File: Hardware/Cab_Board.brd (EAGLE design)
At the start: 152.9 x 71.1 mm, 158 parts, among them J6 3PCV-03-006, SW1 MF-SW-TACT-4.2MM, SW2 MF-SW-TACT-4.2MM, SW3 MF-SW-TACT-4.2MM, U1 P8X32A-Q44, U10 MAX31855KASA+, U11 MAX31855KASA+, U12 G3VM-61GR2(TR05), U13 G3VM-61GR2(TR05), U14 CD74HC595M96, U15 G3VM-61GR2(TR05), U16 CD74HC165M96, U17 G3VM-61GR2(TR05), U18 G3VM-61GR2(TR05), U19 G3VM-61GR2(TR05), U2 G3VM-61GR2(TR05), U20 G3VM-61GR2(TR05), U21 G3VM-61GR2(TR05), U22 G3VM-61GR2(TR05), U23 G3VM-61GR2(TR05), U24 G3VM-61GR2(TR05), U25 G3VM-61GR2(TR05), U26 G3VM-61GR2(TR05), U27 FXOS8700CQR1, U28 ACPL-C870-000E, U29 MAX11613EUA+, U3 G3VM-61GR2(TR05), U30 TPS7B6933QDCYRQ1, U4 MAX31855KASA+, U5 LM22678TJ-5.0/NOPB, U6 ADP3338AKCZ-3.3-RL, U7 CAT24C512WI-GT3, U8 G3VM-61GR2(TR05), U9 MAX31855KASA+, X1 ABMM-6.000MHZ-B2-T

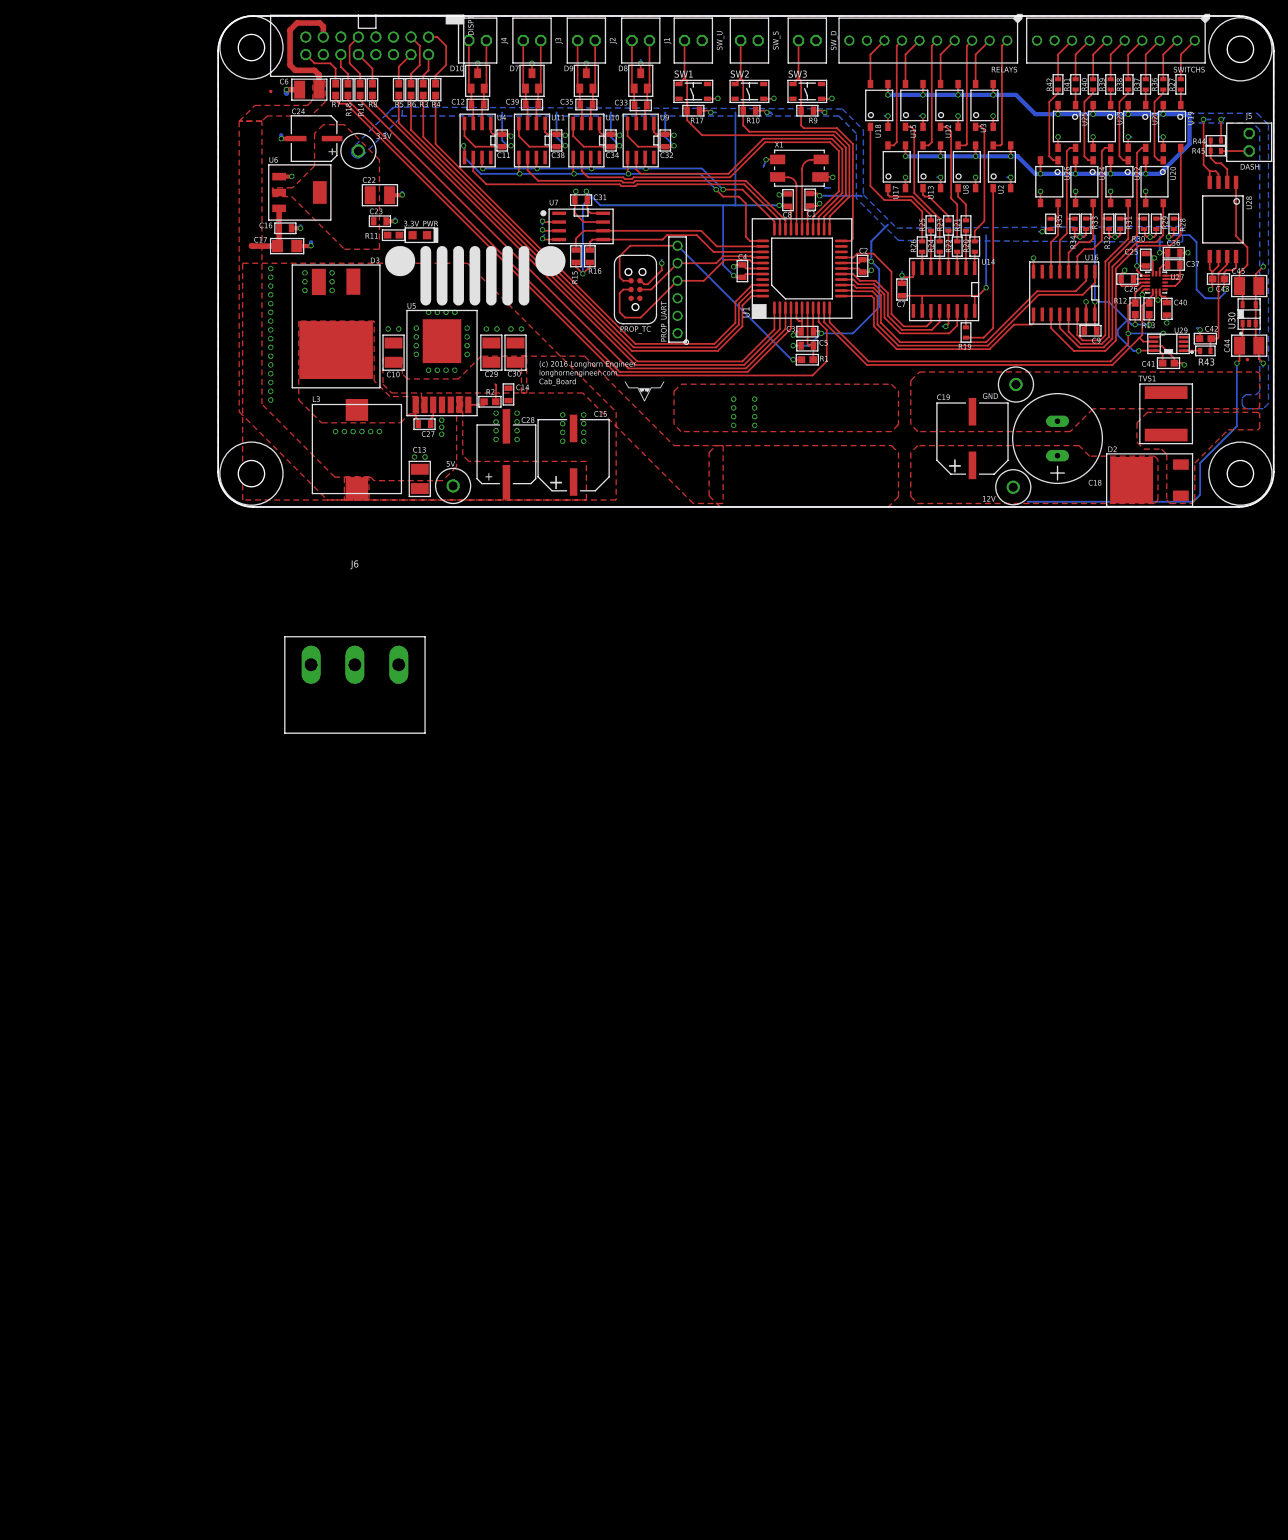
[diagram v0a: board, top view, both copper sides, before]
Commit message: new power input
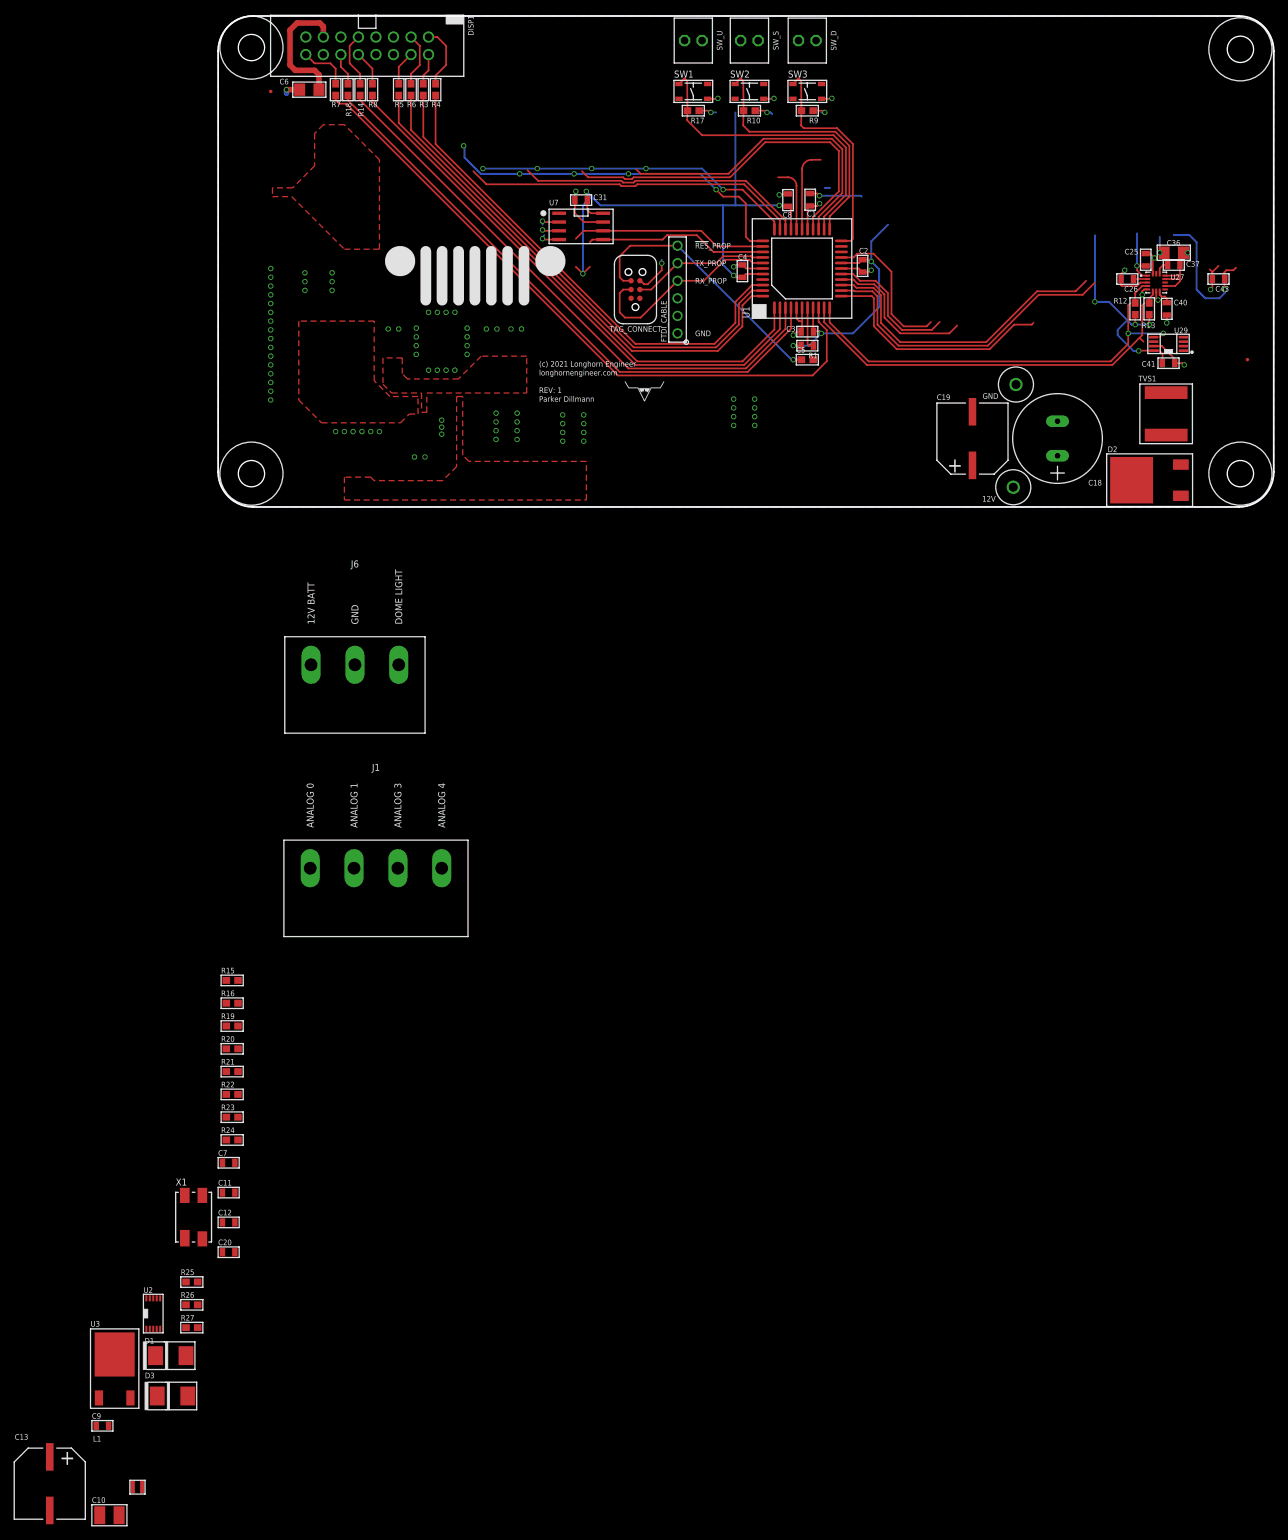
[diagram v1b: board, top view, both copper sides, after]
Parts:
- removed 3.3V, 5V: (no value), PP_Connectors:KEYSTONE_5115-5119
- removed 3.3V_PWR: MF-LED-0805-RED, PP_LED:LED_0805
- removed C14: 1uf, PP_Passives:0805
- removed C15: 1000uF, PP_Passives:10MM_CAP_SMD
- removed C16, C23, C32, C33, C34, C35, C38, C39: 0.1uF, PP_Passives:0805
- removed C17: 10uF, PP_Passives:1206
- removed C22, C44, C45: 10uF, PP_Passives:1210
- removed C24: 47uF, PP_Passives:6.3MM_CAP_SMD
- removed C27: 0.01uF, PP_Passives:0805
- removed C28: 180uF, PP_Passives:8MM_CAP_SMD
- removed C29, C30: 4.7uF, PP_Passives:1210
- removed C42: .1uF, PP_Passives:0603
- removed D10, D7, D8, D9: NUP2105LT1G, PP_Passives:SOT-23
- removed J2, J3, J4, J5: (no value), PP_Connectors:1546215-2
- removed L3: 6.8uH, PP_Passives:IHLP-5050
- removed R11: 330, PP_Passives:0603
- removed R2: 470K, PP_Passives:0603
- removed R28, R29, R30, R31, R32, R33, R34, R35, R36, R37, R38, R39, R40, R41, R42, R43, R44, R45: (no value), MF_Passives:R0603
- removed RELAYS, SWITCHS: (no value), PP_Connectors:1-282834-0
- removed U10, U11, U4, U9: MAX31855KASA+, PP_Sensors:MAX31855_SO-8
- removed U12, U13, U15, U17, U18, U19, U20, U21, U22, U23, U24, U25, U26, U8: G3VM-61GR2(TR05), PP_DigitalIC:G3VM-61GR2
- removed U14: CD74HC595M96, PP_DigitalIC:CD74HC595_SOIC-16
- removed U16: CD74HC165M96, PP_DigitalIC:CD74HC165_SOIC-16
- removed U28: ACPL-C870-000E, PP_AnalogIC:ACPL-C87_SSO-8
- removed U30: TPS7B6933QDCYRQ1, MF_IC_Power:SOT-23-5
- removed U5: LM22678TJ-5.0/NOPB, PP_PowerIC:LM22678_TO-263-EP-7
- removed U6: ADP3338AKCZ-3.3-RL, PP_PowerIC:ADP3338_SOT-223-3
- added C20: 0.1uF, PP_Passives:0805
- added D1: TPSMB33A, PP_Passives:DO-214AA
- added L1: XPL2010-104MLC, PP_Passives:XPL2010
- C13: value 4.7uF -> 470uF; device PP_Passives:1210 -> PP_Passives:10MM_CAP_SMD
- C36: device PP_Passives:0805 -> PP_Passives:1206
- C41, C43: value .1uF -> 0.1uF; device PP_Passives:0603 -> PP_Passives:0805
- C6: device PP_Passives:1210 -> PP_Passives:1206
- C9: value 0.1uF -> 1uF
- D3: value VB20100S-E3/8W -> TPSMB18A; device PP_Passives:D2PAK(TO-263AB) -> PP_Passives:DO-214AA
- FID1, FID2: value (none) -> FIDUCIAL_0.5MM
- J1: value (none) -> 3PCV-04-006; device PP_Connectors:1546215-2 -> PP_Connectors:3PCV-04-006
- R10, R17, R9: device PP_Passives:0805 -> PP_Passives:0603
- R14, R18, R3, R4, R5, R6, R7, R8: value 120 -> 100
- R15, R16: value 10K -> 15K; device PP_Passives:0805 -> PP_Passives:0603
- R19, R20: value (none) -> 15K; device MF_Passives:R0603 -> PP_Passives:0603
- R21, R22, R23, R24: value (none) -> 4.7K; device MF_Passives:R0603 -> PP_Passives:0603
- R25, R26, R27: value (none) -> 100; device MF_Passives:R0603 -> PP_Passives:0603
- SW_D, SW_S, SW_U: value (none) -> 1546215-2
- U2: value G3VM-61GR2(TR05) -> LT8672EMS#PBF; device PP_DigitalIC:G3VM-61GR2 -> PP_PowerIC:LT8672_MSOP-10
- U3: value G3VM-61GR2(TR05) -> IPD100N06S403ATMA2; device PP_DigitalIC:G3VM-61GR2 -> PP_DiscreteSemi:TO-252-3
- X1: value ABMM-6.000MHZ-B2-T -> 6.0MHz
- moved R27 230.1 mm to (-3.81, -118.9), turned to 0 degrees
- moved U3 221.9 mm to (-15.0, -124.5)
- moved C9 213.7 mm to (-16.8, -133.1), turned to 0 degrees
- moved U2 206.7 mm to (-9.40, -116.8)
- moved R25 186.8 mm to (-3.81, -112.3), turned to 0 degrees
- moved R26 186.3 mm to (-3.81, -115.6), turned to 0 degrees
- moved X1 175.5 mm to (-3.56, -102.9)
- moved C10 173.4 mm to (-15.7, -146.1), turned to 0 degrees
- moved C12 165.9 mm to (1.52, -103.6)
- moved R23 165.7 mm to (2.03, -88.4), turned to 0 degrees
- moved R24 165.1 mm to (2.03, -91.7), turned to 0 degrees
- moved R21 162.2 mm to (2.03, -81.8), turned to 0 degrees
- moved R22 161.6 mm to (2.03, -85.1), turned to 0 degrees
- moved C7 159.7 mm to (1.52, -95.0), turned to 0 degrees
- moved R20 158.3 mm to (2.03, -78.5), turned to 0 degrees
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- renumbered PROP_TC to TAG_CONNECT, PROP_UART to FTDI_CABLE
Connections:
- removed net 12V_BATT_ON: C44.1, U30.P$1
- removed net 5V_PWR: C6.1, DISP1.P$13
- removed net CHASSIS_GND: C44.2, C45.2, R44.P$1, U12.P$3, U13.P$3, U15.P$3, U17.P$3, U18.P$3, U19.P$2, U2.P$3, U20.P$2, U21.P$2, U22.P$2, U23.P$2, U24.P$2, U25.P$2, U26.P$2, U28.P$3, U28.P$4, U3.P$3, U30.P$3, U30.P$4, U8.P$3
- removed net EXT_5V: C45.1, U28.P$1, U30.P$5
- removed net IN_OPTO_1: R29.P$1, U16.12, U20.P$4
- removed net IN_OPTO_2: R30.P$1, U16.13, U21.P$4
- removed net IN_OPTO_3: R31.P$1, U16.14, U22.P$4
- removed net IN_OPTO_4: R32.P$1, U16.3, U23.P$4
- removed net IN_OPTO_5: R33.P$1, U16.4, U24.P$4
- removed net IN_OPTO_6: R34.P$1, U16.5, U25.P$4
- removed net IN_OPTO_7: R35.P$1, U16.6, U26.P$4
- removed net N$16: R24.P$2, U15.P$1
- removed net N$17: R25.P$2, U17.P$1
- removed net N$18: R26.P$2, U18.P$1
- removed net N$19: R39.P$1, U23.P$1
- removed net N$20: R40.P$1, U24.P$1
- removed net N$21: R41.P$1, U25.P$1
- removed net N$22: R42.P$1, U26.P$1
- removed net N$23: R27.P$2, SWITCHS.P$1
- removed net N$24: R36.P$2, SWITCHS.P$2
- removed net N$25: R37.P$2, SWITCHS.P$3
- removed net N$26: R38.P$2, SWITCHS.P$4
- removed net N$27: R39.P$2, SWITCHS.P$5
- removed net N$28: R40.P$2, SWITCHS.P$6
- removed net N$29: R41.P$2, SWITCHS.P$7
- removed net N$30: R42.P$2, SWITCHS.P$8
- removed net N$31: R2.2, U5.P$7
- removed net N$32: C42.1, R43.P$1, U28.P$7
- removed net N$33: R44.P$2, R45.P$2, U28.P$2
- removed net N$36: J5.P$1, R45.P$1
- removed net N$5: C27.2, D3.C, L3.2, U5.P$1
- removed net OUT_0: R19.P$1, U14.15
- removed net OUT_1: R20.P$1, U14.1
- removed net OUT_2: R21.P$1, U14.2
- removed net OUT_3: R22.P$1, U14.3
- removed net OUT_4: R23.P$1, U14.4
- removed net OUT_5: R24.P$1, U14.5
- removed net OUT_6: R25.P$1, U14.6
- removed net OUT_7: R26.P$1, U14.7
- removed net RLY_0: RELAYS.P$1, U2.P$4
- removed net RLY_1: RELAYS.P$2, U3.P$4
- removed net RLY_2: RELAYS.P$3, U8.P$4
- removed net RLY_3: RELAYS.P$4, U12.P$4
- removed net RLY_4: RELAYS.P$5, U13.P$4
- removed net RLY_5: RELAYS.P$6, U15.P$4
- removed net RLY_6: RELAYS.P$7, U17.P$4
- removed net RLY_7: RELAYS.P$8, U18.P$4
- removed net SCL_1: R12.1, U1.11, U27.P$4, U29.P$5
- removed net SDA_1: R13.1, U1.10, U27.P$6, U29.P$6
- removed net T+_0: C33.1, D8.1, J1.P$1, U9.3
- removed net T+_1: C35.1, D9.1, J2.P$1, U10.3
- removed net T+_2: C39.1, D7.1, J3.P$1, U11.3
- removed net T+_3: C12.1, D10.1, J4.P$1, U4.3
- removed net T-_0: C33.2, D8.2, J1.P$2, U9.2
- removed net T-_1: C35.2, D9.2, J2.P$2, U10.2
- removed net T-_2: C39.2, D7.2, J3.P$2, U11.2
- removed net T-_3: C12.2, D10.2, J4.P$2, U4.2
- new net P10: U1.11
- new net P9: U1.10
- new net VIN: D1.C, U2.9, U3.3
- net 12V: no longer C10.1, C14.1, C29.1, C30.1, R2.1, U5.P$2
- net 165_CLK: no longer U16.2
- net 165_DATA: no longer U16.9
- net 165_LOAD: no longer U16.1
- net 3.3V: no longer 3.3V.P$1, C11.1, C22.1, C23.1, C24.POS, C32.1, C34.1, C38.1, C7.1, C9.1, R11.1, R15.2, R16.2, R28.P$2, R29.P$2, R30.P$2, R31.P$2, R32.P$2, R33.P$2, R34.P$2, R35.P$2, U10.4, U11.4, U14.10, U14.16, U16.16, U28.P$8, U4.4, U6.2, U6.PAD, U9.4
- net 595_CLK: no longer U14.11
- net 595_DATA: no longer U14.14
- net 595_LAT: no longer U14.12
- net 5V: now also C6.1, DISP1.P$13; no longer 5V.P$1, C13.1, C15.POS, C16.1, C17.1, C28.POS, L3.1, U5.P$6, U6.3
- net A0: now also C7.1, R15.1, R24.2; no longer R43.P$2
- net A1: now also C11.1, R16.1, R23.2
- net A2: now also C12.1, R19.1, R22.2
- net A3: now also C20.1, R20.1, R21.2
- net GND: now also C12.2, C13.NEG, C20.2, D3.C, R21.1, R22.1, R23.1, R24.1, U2.2, U2.4; no longer 3.3V_PWR.CATHODE, C13.2, C14.2, C15.NEG, C16.2, C17.2, C22.2, C23.2, C24.NEG, C28.NEG, C29.2, C30.2, C32.2, C34.2, C38.2, C42.2, C9.2, D10.3, D3.A, D7.3, D8.3, D9.3, U10.1, U11.1, U12.P$2, U13.P$2, U14.13, U14.8, U15.P$2, U16.15, U16.8, U17.P$2, U18.P$2, U19.P$3, U2.P$2, U20.P$3, U21.P$3, U22.P$3, U23.P$3, U24.P$3, U25.P$3, U26.P$3, U28.P$5, U28.P$6, U3.P$2, U4.1, U5.P$4, U5.PAD, U6.1, U8.P$2, U9.1
- net N$1: now also J1.1, R15.2; no longer R28.P$1, U16.11, U19.P$4
- net N$10: now also R25.2, SW_U.P$1; no longer R38.P$1, U22.P$1
- net N$11: now also R26.2, SW_S.P$1; no longer R19.P$2, U2.P$1
- net N$12: now also R27.2, SW_D.P$1; no longer R20.P$2, U3.P$1
- net N$13: now also C10.1, C13.POS, C9.1, L1.P$1, U2.8, U3.PAD; no longer R21.P$2, U8.P$1
- net N$14: now also C9.2, U2.7; no longer R22.P$2, U12.P$1
- net N$15: now also L1.P$2, U2.6; no longer R23.P$2, U13.P$1
- net N$2: now also U2.10, U3.1; no longer C27.1, U5.P$3
- net N$3: now also J1.2, R16.2; no longer R27.P$1, U19.P$1
- net N$4: now also J1.3, R19.2; no longer R36.P$1, U20.P$1
- net N$6: now also J1.4, R20.2; no longer R37.P$1, U21.P$1
- net N$9: now also D1.A, D3.A; no longer 3.3V_PWR.ANODE, R11.2
- net SCL: now also R12.1, U27.P$4, U29.P$5; no longer R15.1
- net SDA: now also R13.1, U27.P$6, U29.P$6; no longer R16.1
- net SW_D: now also R27.1; no longer SW_D.P$1
- net SW_S: now also R26.1; no longer SW_S.P$1
- net SW_U: now also R25.1; no longer SW_U.P$1
- net TC_CS_0: no longer U9.6
- net TC_CS_1: no longer U10.6
- net TC_CS_2: no longer U11.6
- net TC_CS_3: no longer U4.6
- net TC_SCK: no longer U10.5, U11.5, U4.5, U9.5
- net TC_SO: no longer U10.7, U11.7, U4.7, U9.7
- net X0: now also X1.P$3; no longer X1.P$1
- net X1: now also X1.P$1; no longer X1.P$3
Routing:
- net CHASSIS_GND: track 151.9 -> 0.00 mm, vias 20 -> 0
- net 3.3V: track 311.6 -> 205.5 mm, vias 28 -> 18
- net GND: track 187.2 -> 92.8 mm, vias 138 -> 101
- net SCL_1: track 65.8 -> 0.00 mm, vias 2 -> 0
- net SDA_1: track 62.2 -> 0.00 mm
- net P10: track 0.00 -> 60.7 mm, vias 0 -> 2
- net P9: track 0.00 -> 58.1 mm
- net 12V_BATT_ON: track 52.7 -> 0.00 mm, vias 1 -> 0
- net N$1: track 48.9 -> 0.00 mm
- net IN_OPTO_2: track 40.4 -> 0.00 mm
- net IN_OPTO_1: track 36.6 -> 0.00 mm
- net IN_OPTO_3: track 29.3 -> 0.00 mm
- net N$11: track 24.8 -> 0.00 mm
- net IN_OPTO_4: track 22.2 -> 0.00 mm
- net N$18: track 21.9 -> 0.00 mm
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- added copper zone on layer 1, net 5V
- removed copper zone on layer 1, net 12V_BATT
- removed copper zone on layer 1, net 12V_BATT_ON
- removed copper zone on layer 16, net 3.3V
- removed copper zone on layer 1, net 5V_PWR
- removed copper zone on layer 1, net CHASSIS_GND
- removed copper zone on layer 16, net CHASSIS_GND
- removed copper zone on layer 1, net GND

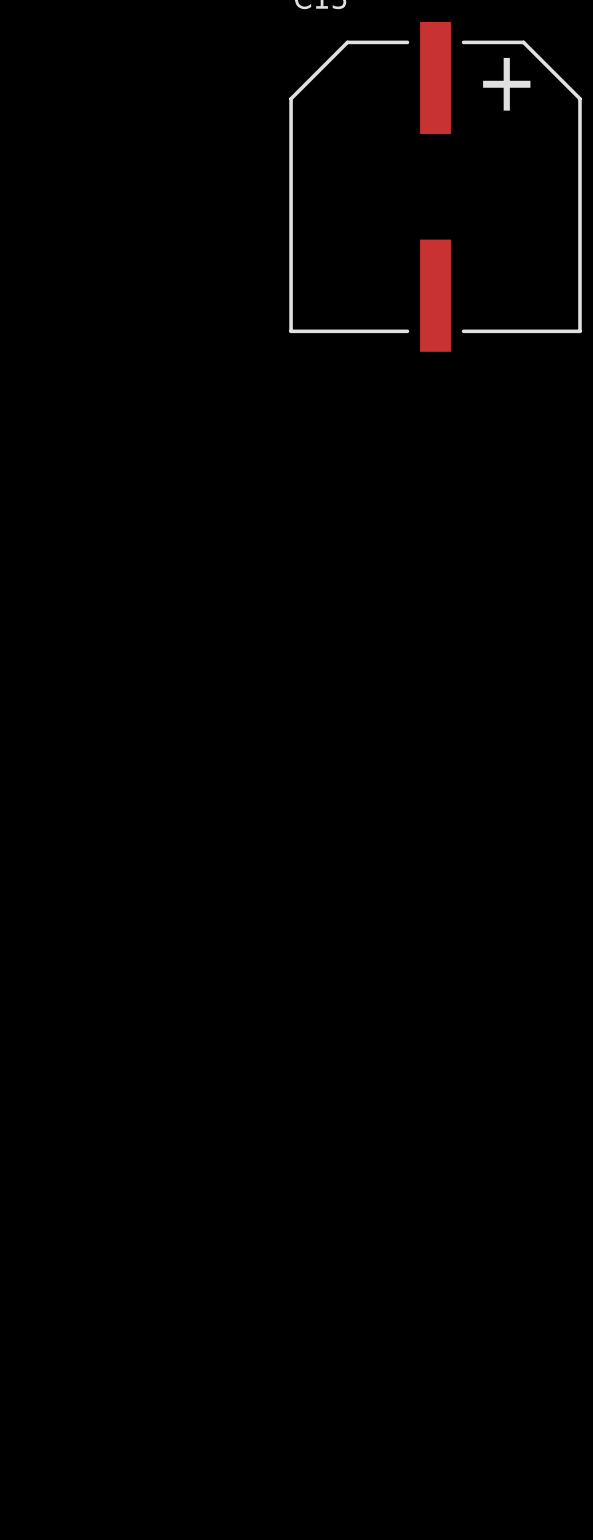
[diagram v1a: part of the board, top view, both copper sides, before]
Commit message: added LT8614
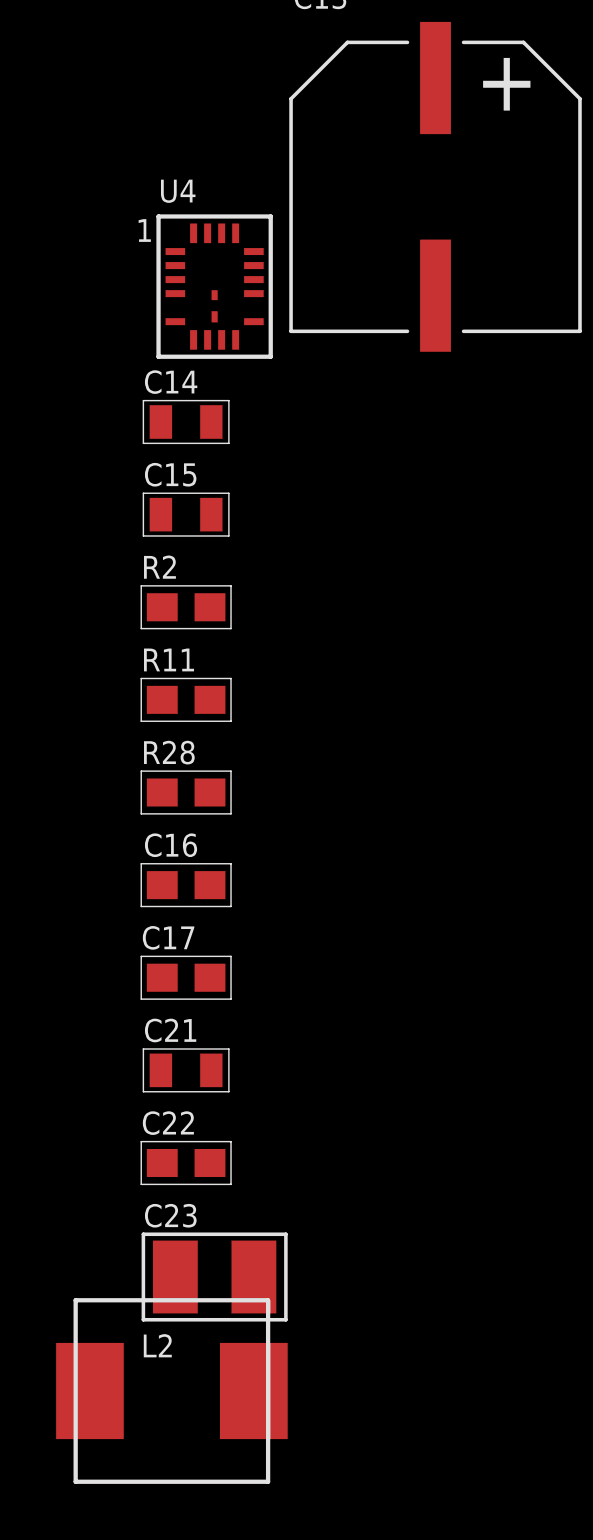
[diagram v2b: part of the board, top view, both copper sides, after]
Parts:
- added C14, C15, C21: 1uF, PP_Passives:0805
- added C16: 4.7pF, PP_Passives:0603
- added C17: 0.1uF, PP_Passives:0603
- added C22: 10nF, PP_Passives:0603
- added C23: 47uF, PP_Passives:1210
- added L2: IHLP2525CZER4R7M01, PP_Passives:IHLP-2525
- added R11: 1M, PP_Passives:0603
- added R2: 41.2K, PP_Passives:0603
- added R28: 412K, PP_Passives:0603
- added U4: LT8614IUDC#PBF, PP_PowerIC:LT8614_QFN-18
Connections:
- new net BST: C17.1, U4.3
- new net FB: C16.2, R11.1, R28.2, U4.20
- new net INTVCC: C21.2, U4.2
- new net RT: R2.2, U4.15
- new net SW: C17.2, L2.P$1, U4.21, U4.22, U4.8, U4.9
- new net TR/SS: C22.2, U4.16
- net 3.3V: now also C16.1, C23.1, L2.P$2, R11.2, U4.1
- net GND: now also C14.2, C15.2, C21.1, C22.1, C23.2, R2.1, R28.1, U4.10, U4.11, U4.18, U4.6, U4.7
- net N$13: now also C14.1, C15.1, U4.13, U4.14, U4.4
